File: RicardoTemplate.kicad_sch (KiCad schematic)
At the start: 35 parts, among them J1 RBUS, U1 ESP32-S3, Y1 40MHz±10ppm

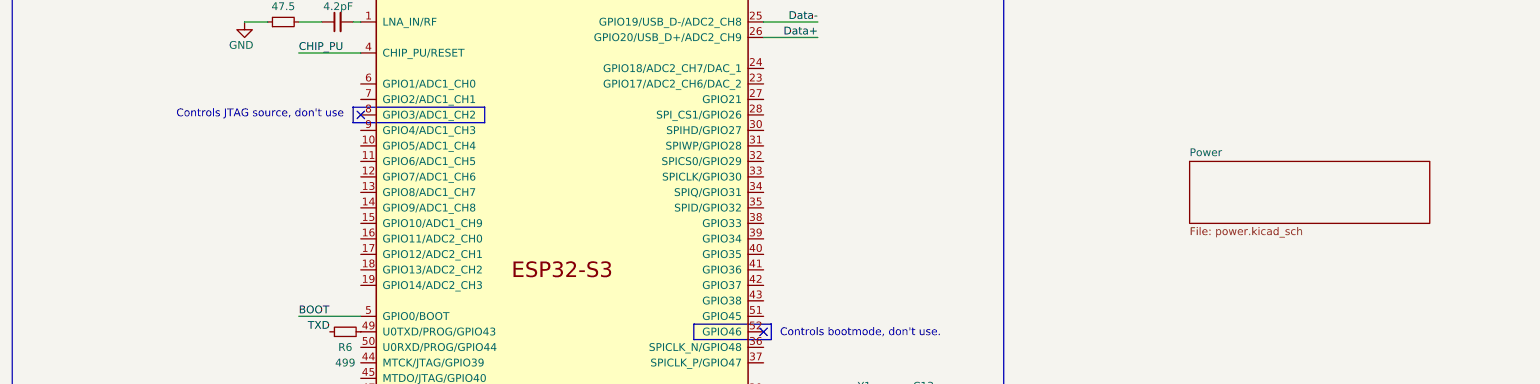
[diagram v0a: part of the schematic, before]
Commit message: updated ideal oring diode and layout
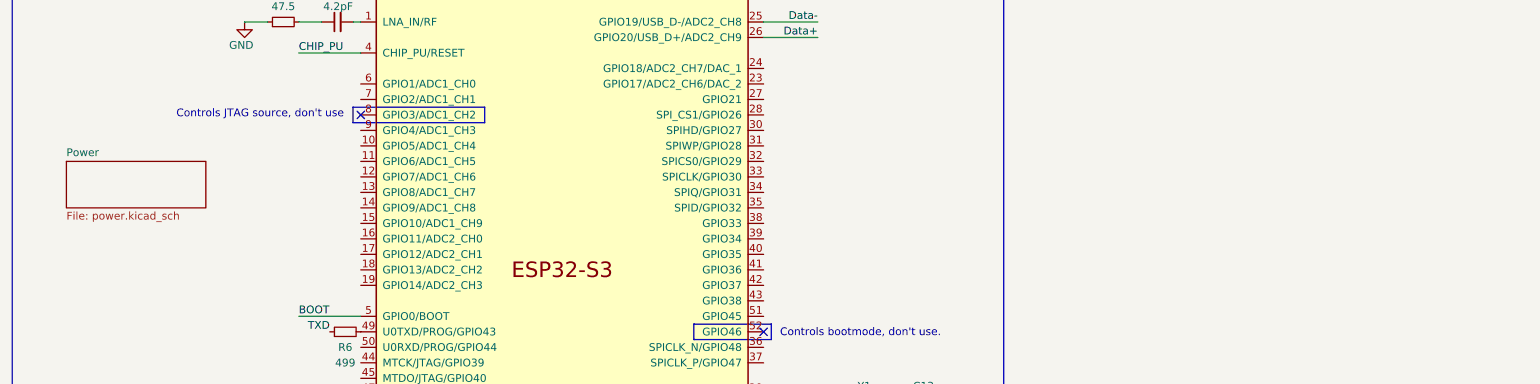
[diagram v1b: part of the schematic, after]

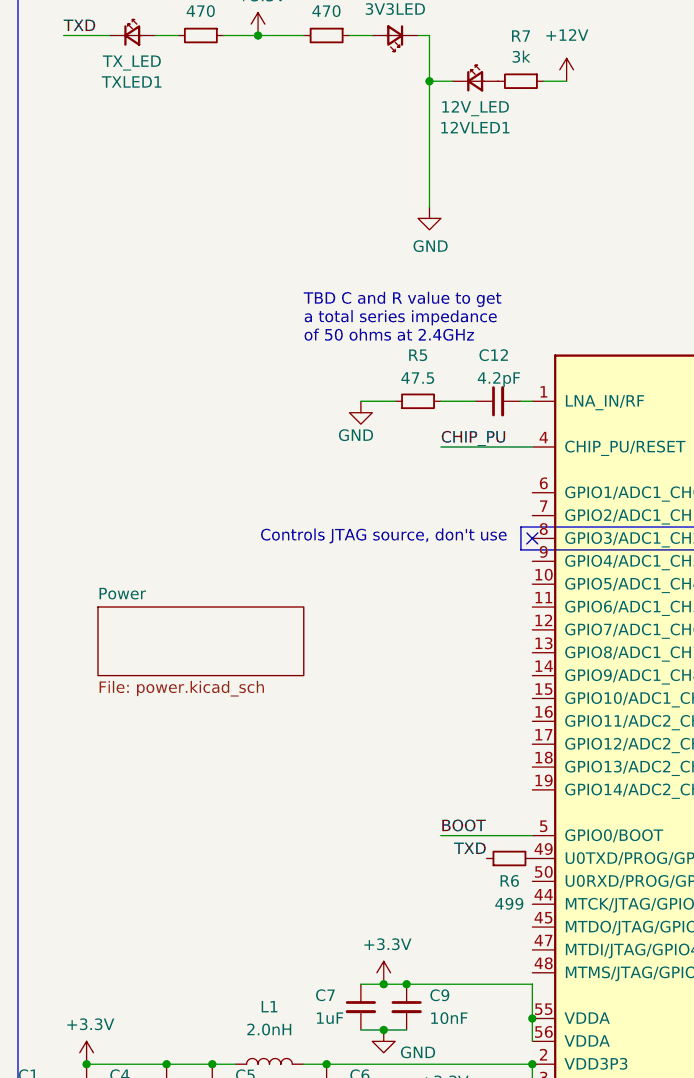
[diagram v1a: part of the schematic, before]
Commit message: Added U0TXD and U0RXD test points
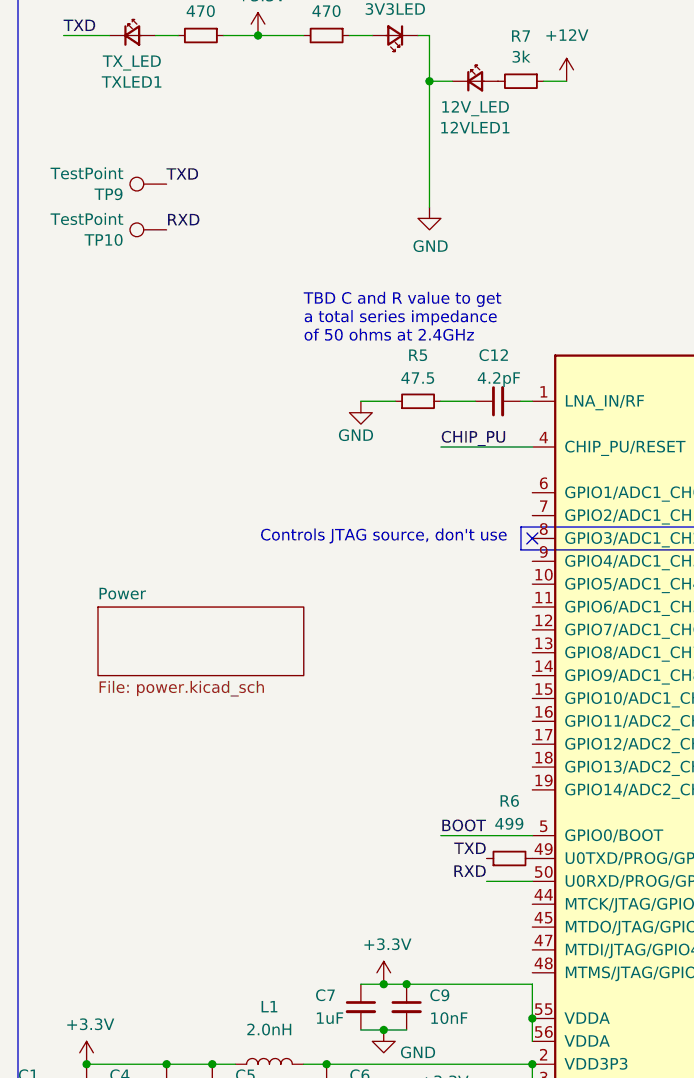
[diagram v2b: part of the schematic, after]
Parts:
- added TP10, TP9: TestPoint, TestPoint:TestPoint_Pad_D1.0mm, symbol Connector:TestPoint
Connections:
- net TXD: now also TP9.1
- net RXD: now reaches U1.50 (U0RXD/PROG/GPIO44)
- net RXD: now also TP10.1
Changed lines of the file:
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@@
+    (stroke (width 0) (type default) (color 0 0 0 0))
+  )
+  (wire (pts (xy 64.77 115.57) (xy 69.85 115.57))
     (stroke (width 0) (type default) (color 0 0 0 0))
   )
@@
     (effects (font (size 1.27 1.27)) (justify left bottom))
   )
+  (label "RXD" (at 29.21 43.18 0)
+    (effects (font (size 1.27 1.27)) (justify left bottom))
+  )
   (label "Data-" (at 99.06 162.56 0)
     (effects (font (size 1.27 1.27)) (justify left bottom))
@@
     (effects (font (size 1.27 1.27)) (justify right bottom))
   )
+  (label "TXD" (at 29.21 38.1 0)
+    (effects (font (size 1.27 1.27)) (justify left bottom))
+  )
   (label "CAN-" (at 115.57 25.4 270)
     (effects (font (size 1.27 1.27)) (justify right bottom))
@@
   )
   (label "BOOT" (at 68.58 165.1 180)
+    (effects (font (size 1.27 1.27)) (justify right bottom))
+  )
+  (label "RXD" (at 64.77 115.57 180)
     (effects (font (size 1.27 1.27)) (justify right bottom))
   )
@@
     (pin "2")
   )
+  (symbol (lib_id "Connector:TestPoint") (at 29.21 38.1 90) (unit 1)
+    (in_bom yes) (on_board yes)
+    (property "Reference" "TP9" (id 0) (at 24.4348 39.2684 90)
+      (effects (font (size 1.27 1.27)) (justify left))
+    )
+    (property "Value" "TestPoint" (id 1) (at 24.4348 36.957 90)
+      (effects (font (size 1.27 1.27)) (justify left))
+    )
+    (property "Footprint" "TestPoint:TestPoint_Pad_D1.0mm" (id 2) (at 29.21 33.02 0)
+      (effects (font (size 1.27 1.27)) hide)
+    )
+    (property "Datasheet" "~" (id 3) (at 29.21 33.02 0)
+      (effects (font (size 1.27 1.27)) hide)
+    )
+    (pin "1")
+  )
   (symbol (lib_id "power:GND") (at 167.64 132.08 0) (unit 1)
     (in_bom yes) (on_board yes)
@@
     )
     (property "Datasheet" "" (id 3) (at 59.69 142.24 0)
+      (effects (font (size 1.27 1.27)) hide)
+    )
+    (pin "1")
+  )
+  (symbol (lib_id "Connector:TestPoint") (at 29.21 43.18 90) (unit 1)
+    (in_bom yes) (on_board yes)
+    (property "Reference" "TP10" (id 0) (at 24.4348 44.3484 90)
+      (effects (font (size 1.27 1.27)) (justify left))
+    )
+    (property "Value" "TestPoint" (id 1) (at 24.4348 42.037 90)
+      (effects (font (size 1.27 1.27)) (justify left))
+    )
+    (property "Footprint" "TestPoint:TestPoint_Pad_D1.0mm" (id 2) (at 29.21 38.1 0)
+      (effects (font (size 1.27 1.27)) hide)
+    )
+    (property "Datasheet" "~" (id 3) (at 29.21 38.1 0)
       (effects (font (size 1.27 1.27)) hide)
     )
@@
   (symbol (lib_id "Device:R_Small") (at 67.31 113.03 90) (unit 1)
     (in_bom yes) (on_board yes)
-    (property "Reference" "R6" (id 0) (at 67.31 115.57 90))
-    (property "Value" "499" (id 1) (at 67.31 118.11 90))
+    (property "Reference" "R6" (id 0) (at 67.31 106.68 90))
+    (property "Value" "499" (id 1) (at 67.31 109.22 90))
     (property "Footprint" "Resistor_SMD:R_0402_1005Metric" (id 2) (at 67.31 113.03 0)
       (effects (font (size 1.27 1.27)) hide)
@@
       (reference "TP8") (unit 1) (value "TestPoint") (footprint "TestPoint:TestPoint_Pad_D1.5mm")
     )
+    (path "/0967eaf7-3e4f-4a2f-9d90-7cb2691f23b6"
+      (reference "TP9") (unit 1) (value "TestPoint") (footprint "TestPoint:TestPoint_Pad_D1.0mm")
+    )
+    (path "/b79adfd9-dbae-480d-ab5a-2a9c412479a2"
+      (reference "TP10") (unit 1) (value "TestPoint") (footprint "TestPoint:TestPoint_Pad_D1.0mm")
+    )
     (path "/00000000-0000-0000-0000-00005db110d6"

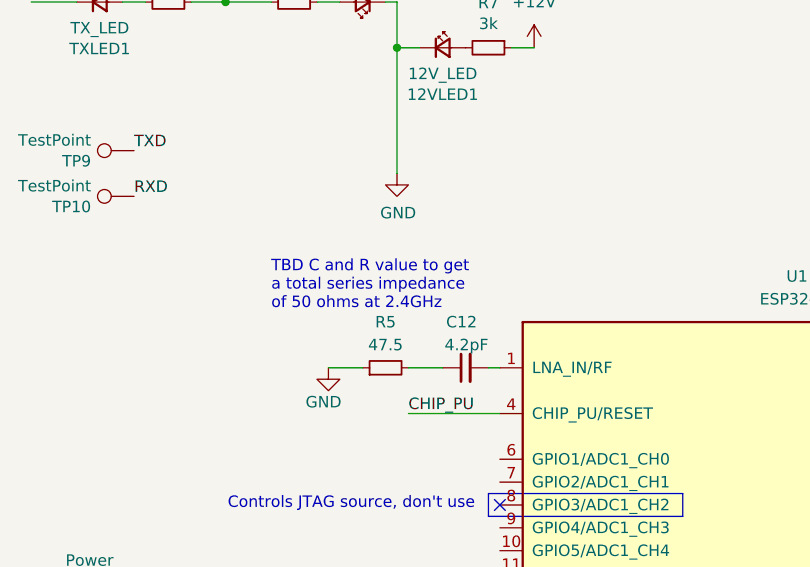
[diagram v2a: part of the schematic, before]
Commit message: changed usb port footprint to the combined SMD/THT one
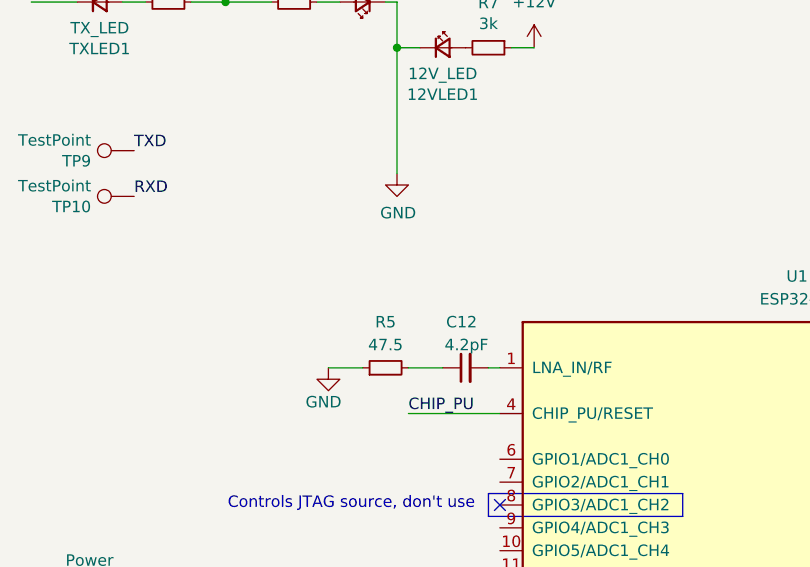
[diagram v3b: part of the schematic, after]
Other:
- note removed: "TBD C and R value to get a total series impedance of 50 ohms at 2.4GHz"
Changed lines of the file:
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@@
-    (effects (font (size 1.27 1.27)) (justify left bottom))
-  )
-  (text "TBD C and R value to get\na total series impedance\nof 50 ohms at 2.4GHz\n"
-    (at 44.45 55.88 0)
     (effects (font (size 1.27 1.27)) (justify left bottom))
   )
@@
     )
     (path "/00000000-0000-0000-0000-000061925999/00000000-0000-0000-0000-000061988c49"
-      (reference "J2") (unit 1) (value "USB_C_Receptacle_USB2.0") (footprint "Connector_USB:USB_C_Receptacle_GCT_USB4085")
+      (reference "J2") (unit 1) (value "USB_C_Receptacle_USB2.0") (footprint "Connector_USB:USB_C_Receptacle_Palconn_UTC16-G")
     )
     (path "/00000000-0000-0000-0000-000061942b9a/deb2b25e-9fb0-448e-88c5-95a67db1d371"
@@
       (reference "TP2") (unit 1) (value "TestPoint") (footprint "TestPoint:TestPoint_Pad_D1.0mm")
     )
-    (path "/00000000-0000-0000-0000-000061925999/00000000-0000-0000-0000-000061ab9568"
-      (reference "TP3") (unit 1) (value "TestPoint") (footprint "TestPoint:TestPoint_Pad_D1.0mm")
-    )
     (path "/48a413b4-b7c2-44ac-971c-583c31b73475/268b5def-07ff-4842-bca3-d3886d833ee9"
       (reference "TP4") (unit 1) (value "TestPoint") (footprint "TestPoint:TestPoint_Pad_D1.5mm")
@@
     )
     (path "/48a413b4-b7c2-44ac-971c-583c31b73475/067fcbdc-a037-45c7-a11e-fa748d280ce6"
-      (reference "U3") (unit 1) (value "LM66200DRLR") (footprint "SOTFL50P160X60-8N")
+      (reference "U3") (unit 1) (value "LM66200DRLR") (footprint "iclr:SOTFL50P160X60-8N")
     )
     (path "/48a413b4-b7c2-44ac-971c-583c31b73475/9e553dc0-c0ec-45f7-ad87-8ecb647a8da4"

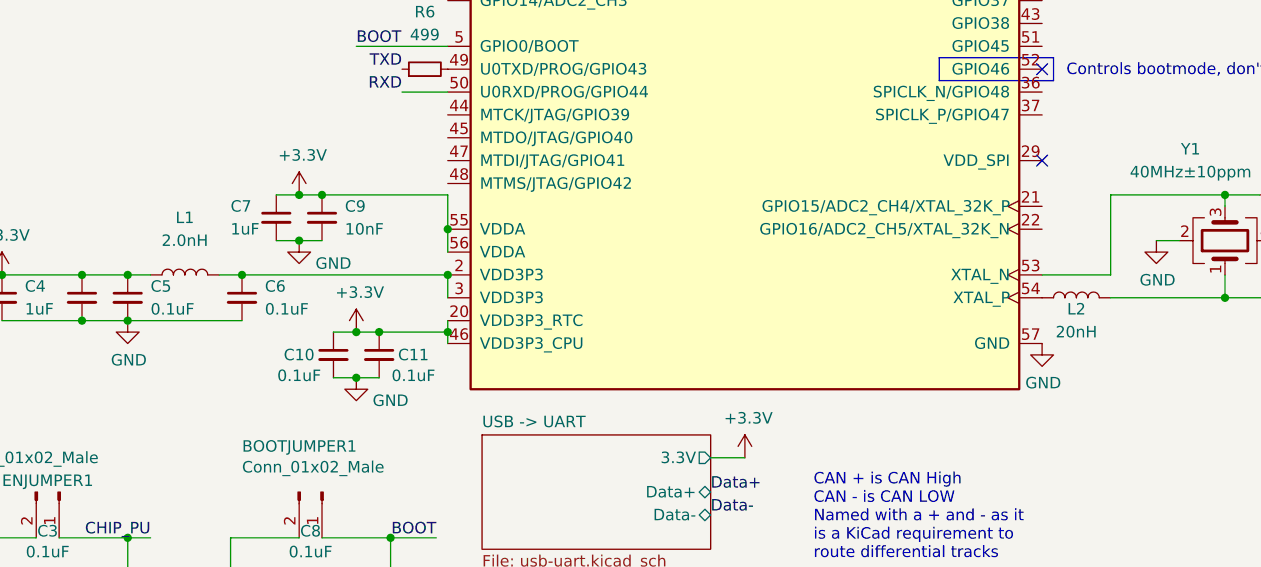
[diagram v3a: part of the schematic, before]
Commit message: updated some schematic values
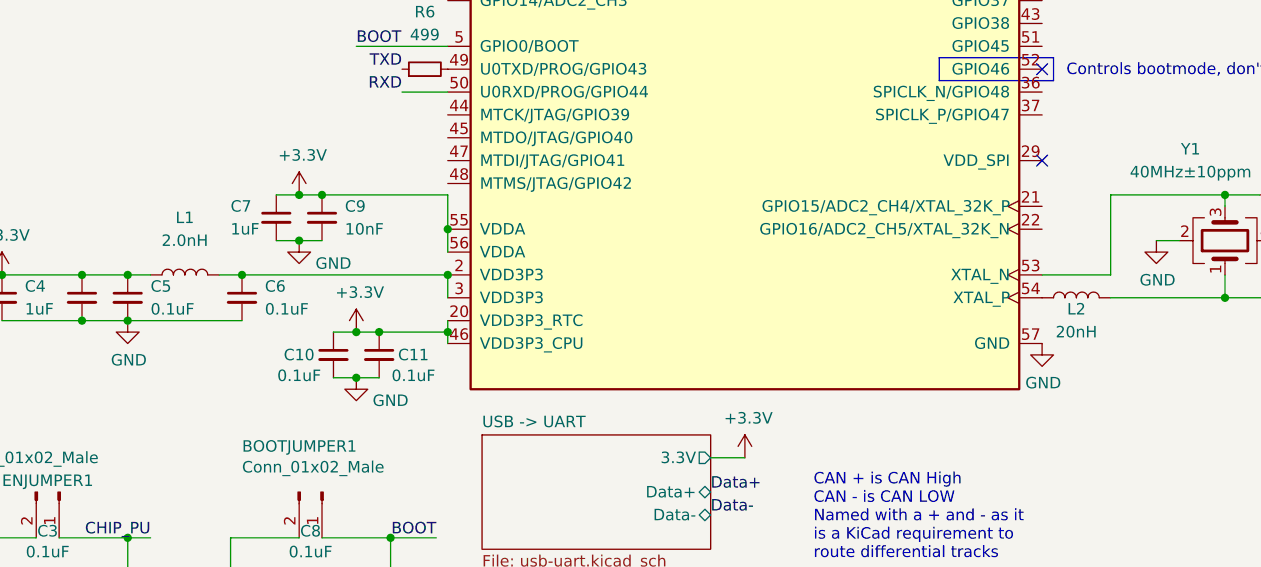
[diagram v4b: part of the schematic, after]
